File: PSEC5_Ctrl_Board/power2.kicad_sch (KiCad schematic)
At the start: 24 parts

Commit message: Minor Schematic Changes, ERC still haunts me :(
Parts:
- added B1, E1, F1: LP38501TS-ADJ/NOPB, TS5B, symbol PSEC5_ctrlbd:LP38501TS-ADJ_NOPB
- added C14, C15, C16, C2, C3, C4, C5: 10u, Capacitor_SMD:C_0603_1608Metric, symbol Device:C_Small
- added R10: 44.5k, Resistor_SMD:R_0603_1608Metric, symbol Device:R_Small_US
- added R11, R12, R14, R15, R17, R2: 10k, Resistor_SMD:R_0603_1608Metric, symbol Device:R_Small_US
- added R13: 31.3k, Resistor_SMD:R_0603_1608Metric, symbol Device:R_Small_US
- added R16: 19.7k, Resistor_SMD:R_0603_1608Metric, symbol Device:R_Small_US
- added TP21, TP23, TP25: GND, symbol Connector:TestPoint
- added TP22: 3V3_IO, symbol Connector:TestPoint
- added TP24: 2V5_IO, symbol Connector:TestPoint
- added TP26: 1V8_IO, symbol Connector:TestPoint
- R45, R60: value 31.3k -> 19.7k
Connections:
- net GND: now also B1.3 (GND), B1.6 (TAB), C14.2, C15.2, C16.2, C2.2, C3.2, C4.2, C5.2, E1.3 (GND), E1.6 (TAB), F1.3 (GND), F1.6 (TAB), R11.2, R14.2, R17.2, TP21.1, TP23.1, TP25.1
- net VDD_BUCK_5V: now also B1.1 (EN), B1.2 (IN), C14.1, C15.1, C16.1, C2.1, C3.1, C4.1, C5.1, E1.1 (EN), E1.2 (IN), F1.1 (EN), F1.2 (IN), R12.1, R12.2, R15.1, R15.2, R2.1, R2.2
- new net: F1.5 (ADJ), R13.2, R14.1
- new net: E1.5 (ADJ), R10.2, R11.1
- new net: B1.5 (ADJ), R16.2, R17.1
- new net 1V8_IO: B1.4 (OUT), R16.1, TP26.1
- new net 2V5_IO: F1.4 (OUT), R13.1, TP24.1
- new net 3V3_IO: E1.4 (OUT), R10.1, TP22.1
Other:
- note added: "1V8 to IO"
- note added: "2V5 to IO"
- note added: "3V3 to IO"
- note added: "Vmin = 2.413V Vtyp = 2.500V Vmax = 2.588V"
- note added: "Vmin = 3.19V Vtyp = 3.30V Vmax = 3.435V"
- moved on the sheet: C, D, R62, R63, R64, R69, R70, R71, TP11, TP12, TP15, TP16

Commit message: Some more Changes
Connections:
- net VDD_BUCK_5V: no longer A.1 (EN), A.2 (IN), B1.1 (EN), B1.2 (IN), C.1 (EN), C.2 (IN), C15.1, C16.1, C2.1, C4.1, C5.1, D.1 (EN), D.2 (IN), F1.1 (EN), F1.2 (IN), R12.1, R12.2, R15.1, R15.2, R59.1, R59.2, R62.1, R62.2, R69.1, R69.2
- new net 3V3_FEED: A.1 (EN), A.2 (IN), B1.1 (EN), B1.2 (IN), C.1 (EN), C.2 (IN), C15.1, C16.1, C2.1, C4.1, C5.1, D.1 (EN), D.2 (IN), F1.1 (EN), F1.2 (IN), R12.1, R12.2, R15.1, R15.2, R59.1, R59.2, R62.1, R62.2, R69.1, R69.2
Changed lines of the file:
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@@
 	)
 	(junction
-		(at 46.99 100.33)
-		(diameter 0)
-		(color 0 0 0 0)
-	)
-	(junction
 		(at 374.65 41.91)
 		(diameter 0)
@@
 	(wire
 		(pts
-			(xy 46.99 100.33) (xy 50.8 100.33)
-		)
-		(stroke
-			(width 0)
-			(type default)
-		)
-	)
-	(wire
-		(pts
 			(xy 45.72 36.83) (xy 45.72 39.37)
 		)
@@
 	(wire
 		(pts
-			(xy 41.91 100.33) (xy 46.99 100.33)
+			(xy 41.91 100.33) (xy 50.8 100.33)
 		)
 		(stroke
@@
 		)
 	)
-	(global_label "VDD_BUCK_5V"
+	(global_label "3V3_FEED"
 		(shape input)
 		(at 35.56 46.99 180)
@@
 		)
 		(property "Intersheetrefs" "${INTERSHEET_REFS}"
-			(at 19.5724 46.99 0)
+			(at 23.443 46.99 0)
 			(effects
 				(font
@@
 		)
 	)
-	(global_label "VDD_BUCK_5V"
+	(global_label "3V3_FEED"
 		(shape input)
 		(at 299.72 52.07 180)
@@
 		)
 		(property "Intersheetrefs" "${INTERSHEET_REFS}"
-			(at 283.7324 52.07 0)
+			(at 287.603 52.07 0)
 			(effects
 				(font
@@
 		)
 	)
-	(global_label "VDD_BUCK_5V"
+	(global_label "3V3_FEED"
 		(shape input)
 		(at 299.72 113.03 180)
@@
 		)
 		(property "Intersheetrefs" "${INTERSHEET_REFS}"
-			(at 283.7324 113.03 0)
+			(at 287.603 113.03 0)
 			(effects
 				(font
@@
 		)
 	)
-	(global_label "VDD_BUCK_5V"
+	(global_label "3V3_FEED"
 		(shape input)
 		(at 168.91 109.22 180)
@@
 		)
 		(property "Intersheetrefs" "${INTERSHEET_REFS}"
-			(at 152.9224 109.22 0)
+			(at 156.793 109.22 0)
 			(effects
 				(font
@@
 		)
 	)
-	(global_label "VDD_BUCK_5V"
+	(global_label "3V3_FEED"
 		(shape input)
 		(at 168.91 170.18 180)
@@
 		)
 		(property "Intersheetrefs" "${INTERSHEET_REFS}"
-			(at 152.9224 170.18 0)
+			(at 156.793 170.18 0)
 			(effects
 				(font
@@
 		)
 	)
-	(global_label "VDD_BUCK_5V"
+	(global_label "3V3_FEED"
 		(shape input)
 		(at 299.72 102.87 180)
@@
 		)
 		(property "Intersheetrefs" "${INTERSHEET_REFS}"
-			(at 283.7324 102.87 0)
+			(at 287.603 102.87 0)
 			(effects
 				(font
@@
 		)
 	)
-	(global_label "VDD_BUCK_5V"
+	(global_label "3V3_FEED"
 		(shape input)
 		(at 168.91 160.02 180)
@@
 		)
 		(property "Intersheetrefs" "${INTERSHEET_REFS}"
-			(at 152.9224 160.02 0)
+			(at 156.793 160.02 0)
 			(effects
 				(font
@@
 		)
 	)
-	(global_label "VDD_BUCK_5V"
+	(global_label "3V3_FEED"
 		(shape input)
 		(at 35.56 36.83 180)
@@
 		)
 		(property "Intersheetrefs" "${INTERSHEET_REFS}"
-			(at 19.5724 36.83 0)
+			(at 23.443 36.83 0)
 			(effects
 				(font
@@
 		)
 	)
-	(global_label "VDD_BUCK_5V"
+	(global_label "3V3_FEED"
 		(shape input)
 		(at 299.72 41.91 180)
@@
 		)
 		(property "Intersheetrefs" "${INTERSHEET_REFS}"
-			(at 283.7324 41.91 0)
+			(at 287.603 41.91 0)
 			(effects
 				(font
@@
 		)
 	)
-	(global_label "VDD_BUCK_5V"
+	(global_label "3V3_FEED"
 		(shape input)
 		(at 168.91 99.06 180)
@@
 		)
 		(property "Intersheetrefs" "${INTERSHEET_REFS}"
-			(at 152.9224 99.06 0)
+			(at 156.793 99.06 0)
 			(effects
 				(font
@@
 					(unit 1)
 				)
-			)
-		)
-	)
-	(symbol
-		(lib_id "power:PWR_FLAG")
-		(at 46.99 100.33 0)
-		(unit 1)
-		(exclude_from_sim no)
-		(in_bom yes)
-		(on_board yes)
-		(dnp no)
-		(fields_autoplaced yes)
-		(property "Reference" "#FLG02"
-			(at 46.99 98.425 0)
-			(effects
-				(font
-					(size 1.27 1.27)
-				)
-				(hide yes)
-			)
-		)
-		(property "Value" "PWR_FLAG"
-			(at 46.99 95.25 0)
-			(effects
-				(font
-					(size 1.27 1.27)
-				)
-			)
-		)
-		(property "Footprint" ""
-			(at 46.99 100.33 0)
-			(effects
-				(font
-					(size 1.27 1.27)
-				)
-				(hide yes)
-			)
-		)
-		(property "Datasheet" "~"
-			(at 46.99 100.33 0)
-			(effects
-				(font
-					(size 1.27 1.27)
-				)
-				(hide yes)
-			)
-		)
-		(property "Description" "Special symbol for telling ERC where power comes from"
-			(at 46.99 100.33 0)
-			(effects
-				(font
-					(size 1.27 1.27)
-				)
-				(hide yes)
-			)
-		)
-		(pin "1"
-		)
-		(instances
-			(project "PSEC5_Ctrl_Board"
-				(path "/165f2ae6-d522-4adf-a6c4-bb137b209d33/ba7b9281-d70b-432c-9c7d-bfda745e0250"
-					(reference "#FLG02")
-					(unit 1)
-				)

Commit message: ERC "Done" (4 errors left) Schematic "Done"
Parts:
- removed C4: 10u, Capacitor_SMD:C_0603_1608Metric, symbol Device:C_Small
- removed D: LP38501TS-ADJ/NOPB, TS5B, symbol PSEC5_ctrlbd:LP38501TS-ADJ_NOPB
- removed R69, R71: 10k, Resistor_SMD:R_0603_1608Metric, symbol Device:R_Small_US
- removed R70: 6.52k, Resistor_SMD:R_0603_1608Metric, symbol Device:R_Small_US
- removed TP11: GND, symbol Connector:TestPoint
- removed TP12: 1V0_Eth, symbol Connector:TestPoint
- added C22, C23, C24, C25, C26, C27: 10u, Capacitor_SMD:C_0603_1608Metric, symbol Device:C_Small
- renumbered A to LDO1, B to LDO2, C to LDO3, E1 to LDO4, F1 to LDO5, B1 to LDO6
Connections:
- net 1V2_Banks: now also C24.1
- net 1V8_ADC: now also C23.1
- net 1V8_Banks: now also C22.1
- net 1V8_IO: now also C25.1
- net 2V5_IO: now also C26.1
- net 3V3_FEED: no longer LDO1.1 (EN), LDO3.1 (EN), LDO5.1 (EN), LDO6.1 (EN), R12.2, R15.2, R59.2, R62.2
- net 3V3_IO: now also C27.1
- net GND: now also C22.2, C23.2, C24.2, C25.2, C26.2, C27.2
- net VDD_BUCK_5V: no longer LDO2.1 (EN), LDO4.1 (EN), R2.2, R44.2
- new net: LDO3.1 (EN), R62.2
- new net: LDO2.1 (EN), R44.2
- new net: LDO6.1 (EN), R15.2
- new net: LDO4.1 (EN), R2.2
- new net: LDO5.1 (EN), R12.2
- new net: LDO1.1 (EN), R59.2
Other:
- note removed: "1V0 to Ethernet"
- note removed: "Vmin = 0.965V Vtyp = 1.000V Vmax = 1.039V"
- moved on the sheet: TP13, TP15, TP21, TP23, TP25, TP9

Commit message: Changes
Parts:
- removed C16, C25: 10u, Capacitor_SMD:C_0603_1608Metric, symbol Device:C_Small
- removed LDO6: LP38501TS-ADJ/NOPB, TS5B, symbol PSEC5_ctrlbd:LP38501TS-ADJ_NOPB
- removed R15, R17: 10k, Resistor_SMD:R_0603_1608Metric, symbol Device:R_Small_US
- removed R16: 19.7k, Resistor_SMD:R_0603_1608Metric, symbol Device:R_Small_US
- removed TP25: GND, symbol Connector:TestPoint
- removed TP26: 1V8_IO, symbol Connector:TestPoint
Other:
- note removed: "1V8 to IO"

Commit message: My PC is fading, pushing in case it dies
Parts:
- added C108: 470p, Capacitor_SMD:C_0603_1608Metric, symbol Device:C_Small
- added C16: 47u, Capacitor_SMD:C_0603_1608Metric, symbol Device:C_Small
- added C25, C76, C81: 0.1u, Capacitor_SMD:C_0603_1608Metric, symbol Device:C_Small
- added C74: 4.7u, Capacitor_SMD:C_0603_1608Metric, symbol Device:C_Small
- added C77: 2.2n, Capacitor_SMD:C_0603_1608Metric, symbol Device:C_Small
- added C80: 1.8n, Capacitor_SMD:C_0603_1608Metric, symbol Device:C_Small
- added C93, C99: 64u, Capacitor_SMD:C_0603_1608Metric, symbol Device:C_Small
- added C97: 1u, Capacitor_SMD:C_0603_1608Metric, symbol Device:C_Small
- added C98: 33n, Capacitor_SMD:C_0603_1608Metric, symbol Device:C_Small
- added J7: 1766343, Connector_Phoenix_GMSTB:PhoenixContact_GMSTBA_2,5_2-G_1x02_P7.50mm_Horizontal, symbol PSEC5_ctrlbd:1766343
- added L2: 4.7u, symbol Device:L_Small
- added R15: 560k, Resistor_SMD:R_0603_1608Metric, symbol Device:R_Small_US
- added R16: 3.3, Resistor_SMD:R_0603_1608Metric, symbol Device:R_Small_US
- added R17: 8.66k, Resistor_SMD:R_0603_1608Metric, symbol Device:R_Small_US
- added R72: 0R, Resistor_SMD:R_0603_1608Metric, symbol Device:R_Small_US
- added R77: DNP, Resistor_SMD:R_0603_1608Metric, symbol Device:R_Small_US
- added R89: 102k, Resistor_SMD:R_0603_1608Metric, symbol Device:R_Small_US
- added R90: 21.25k, Resistor_SMD:R_0603_1608Metric, symbol Device:R_Small_US
- added R91: 232k, Resistor_SMD:R_0603_1608Metric, symbol Device:R_Small_US
- added R92: 2k, Resistor_SMD:R_0603_1608Metric, symbol Device:R_Small_US
- added R93: 60.4k, Resistor_SMD:R_0603_1608Metric, symbol Device:R_Small_US
- added R94: 52.3k, Resistor_SMD:R_0603_1608Metric, symbol Device:R_Small_US
- added R95: 10k, Resistor_SMD:R_0603_1608Metric, symbol Device:R_Small_US
- added TP25: 5V_BUCK, TestPoint:TestPoint_Bridge_Pitch2.0mm_Drill0.7mm, symbol Connector:TestPoint
- added TP26: 5V_PGOOD, TestPoint:TestPoint_Bridge_Pitch2.0mm_Drill0.7mm, symbol Connector:TestPoint
- added U13: SIC473ED-T1-GE3, PowerPAK_MLP55-27L_VIS, symbol PSEC5_ctrlbd:SIC473ED-T1-GE3
- LDO1, LDO2, LDO3, LDO4, LDO5: footprint TS5B -> ul_LP38501TS-ADJ-NOPB:TS5B
- TP10, TP13, TP14, TP15, TP16, TP21, TP22, TP23, TP24, TP9: footprint (none) -> TestPoint:TestPoint_Bridge_Pitch2.0mm_Drill0.7mm
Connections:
- net GND: now also C108.2, C25.2, C97.2, C98.2, R77.2, R92.2, R93.2, R94.2, R95.2, U13.23 (AGND), U13.28 (AGND)
- net VDD_BUCK_5V: now also C15.1, LDO5.2 (IN), R12.1; no longer C3.1, LDO2.2 (IN), R44.1
- net 3V3_FEED renamed VDD_BUCK_2V5
- net VDD_BUCK_2V5: now also C3.1, LDO2.2 (IN), R44.1, C80.2, C81.1, C93.1, C99.1, L2.2, R90.1, TP25.1; no longer C15.1, LDO5.2 (IN), R12.1
- new net: C97.1, R72.1, R89.1, U13.26 (VDD)
- new net: R93.1, U13.25 (ILIMIT)
- new net: C77.1, U13.20 (VSNS)
- new net: C77.2, C80.1, R17.2
- new net: R90.2, R91.1, R95.1, U13.21 (COMP), U13.22 (VFB)
- new net: R92.1, U13.27 (MODE)
- new net: C16.1, C25.1, J7.1, R15.1, U13.1 (VCIN), U13.29 (VIN), U13.7 (VIN), U13.8 (VIN)
- new net: C98.1, U13.19 (SS)
- new net: L2.1, R17.1, U13.12 (SW), U13.13 (SW), U13.14 (SW)
- new net: C76.1, R16.2
- new net: C76.2, U13.4 (BOOT)
- new net: C74.1, U13.16 (VDRV)
- new net: R72.2, U13.18 (ULTRASONIC)
- new net: R94.1, U13.24 (FSW)
- new net: R16.1, U13.5 (PHASE), U13.6 (PHASE)
- new net: C108.1, R91.2
- new net 2V5_PGOOD: R89.2, TP26.1, U13.2 (PGOOD)
- new net 5V_EN: R15.2, R77.1, U13.3 (EN)
- new net GNDPWR: C16.2, C74.2, C81.2, C93.2, C99.2, U13.10 (PGND), U13.11 (PGND), U13.17 (PGND), U13.30 (PGND), U13.9 (PGND)
- no-connect marks 0 -> 2
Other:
- note added: "2V5 Buck Supply To 1V8 and 1V2 LDO's"
- note added: "Physical Connector (Plug) 6V-55V"

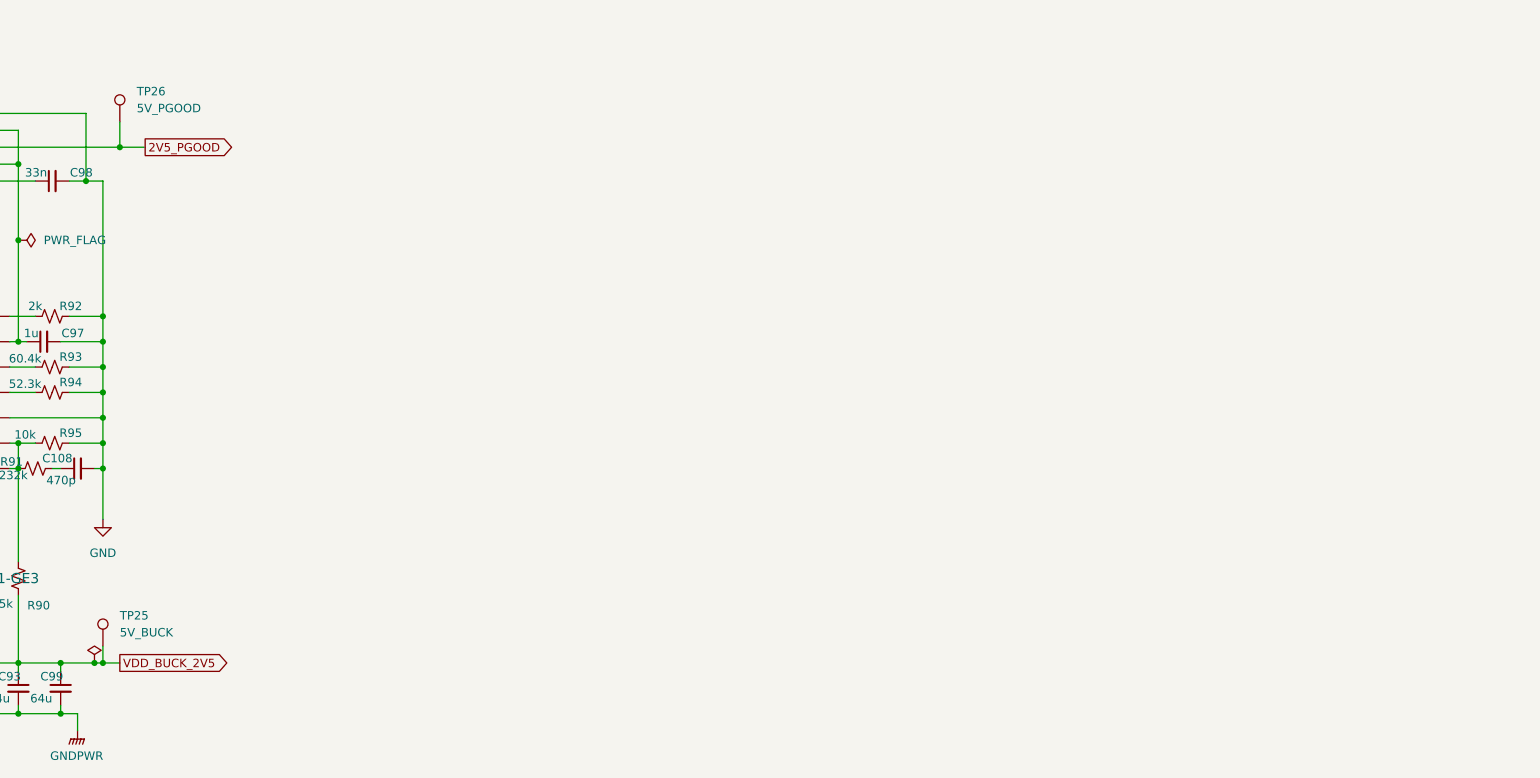
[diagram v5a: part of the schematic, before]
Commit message: Changed Buck Regulators to external
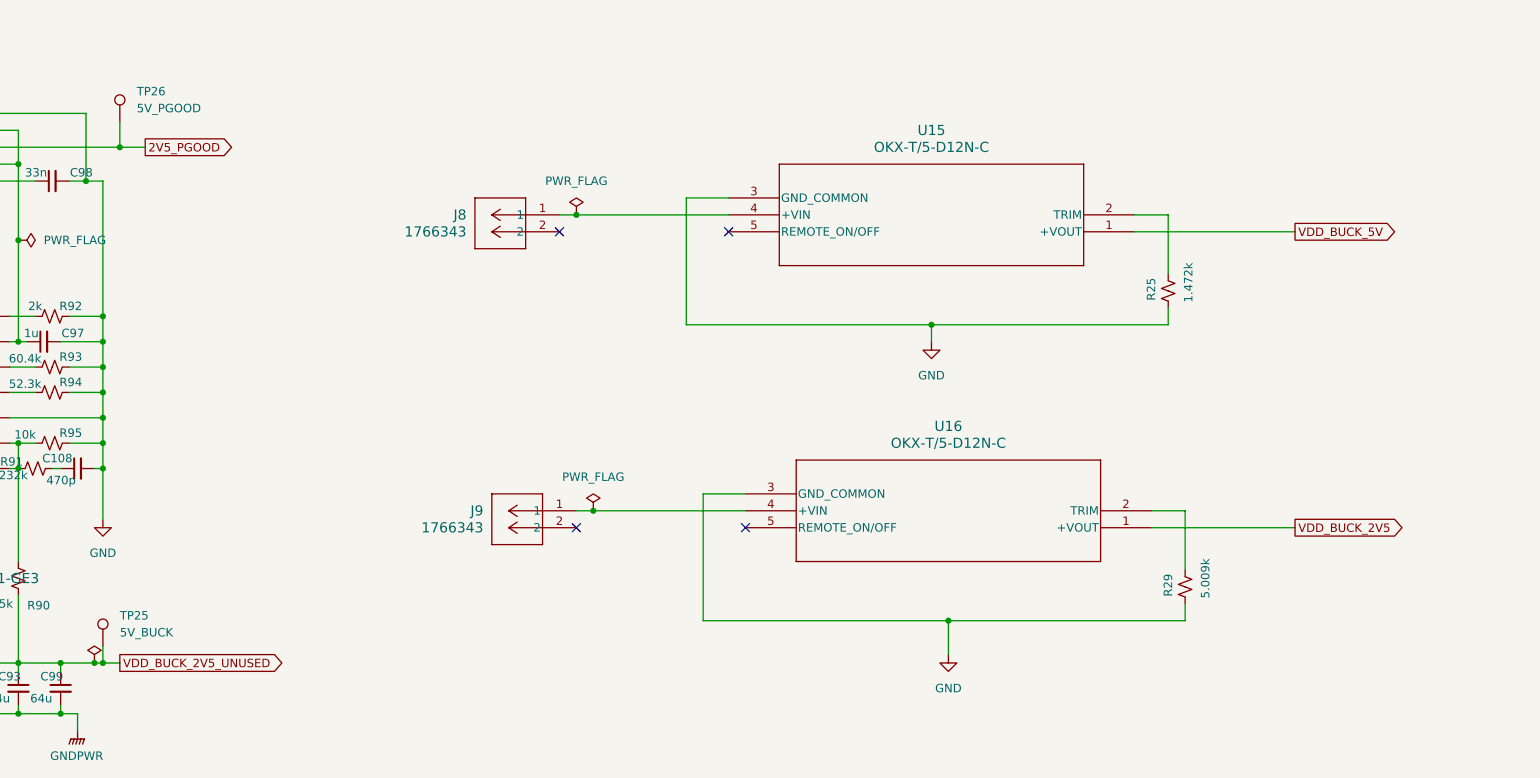
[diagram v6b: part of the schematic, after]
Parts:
- added J8, J9: 1766343, Connector_Phoenix_GMSTB:PhoenixContact_GMSTBA_2,5_2-G_1x02_P7.50mm_Horizontal, symbol PSEC5_ctrlbd:1766343
- added R25: 1.472k, Resistor_SMD:R_0603_1608Metric, symbol Device:R_Small_US
- added R29: 5.009k, Resistor_SMD:R_0603_1608Metric, symbol Device:R_Small_US
- added U15, U16: OKX-T/5-D12N-C, OKX-T/5-D12N-C_MUR, symbol PSEC5_ctrlbd:OKX-T_5-D12N-C
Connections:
- net GND: now also R25.1, R29.1, U15.3 (GND_COMMON), U16.3 (GND_COMMON)
- net VDD_BUCK_2V5: now also U16.1 (+VOUT); no longer C80.2, C81.1, C93.1, C99.1, L2.2, R90.1, TP25.1
- net VDD_BUCK_5V: now also U15.1 (+VOUT)
- new net: R29.2, U16.2 (TRIM)
- new net: J9.1, U16.4 (+VIN)
- new net: R25.2, U15.2 (TRIM)
- new net: J8.1, U15.4 (+VIN)
- new net VDD_BUCK_2V5_UNUSED: C80.2, C81.1, C93.1, C99.1, L2.2, R90.1, TP25.1
- no-connect marks 2 -> 6
